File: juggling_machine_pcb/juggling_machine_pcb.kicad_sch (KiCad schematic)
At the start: 14 parts, among them J1 Conn_01x08, J2 Conn_01x08, J3 Conn_01x08, J4 Conn_01x08, J5 servo 1, J6 servo 2, J7 24v input, J8 5v input, J9 24v out for input to buck

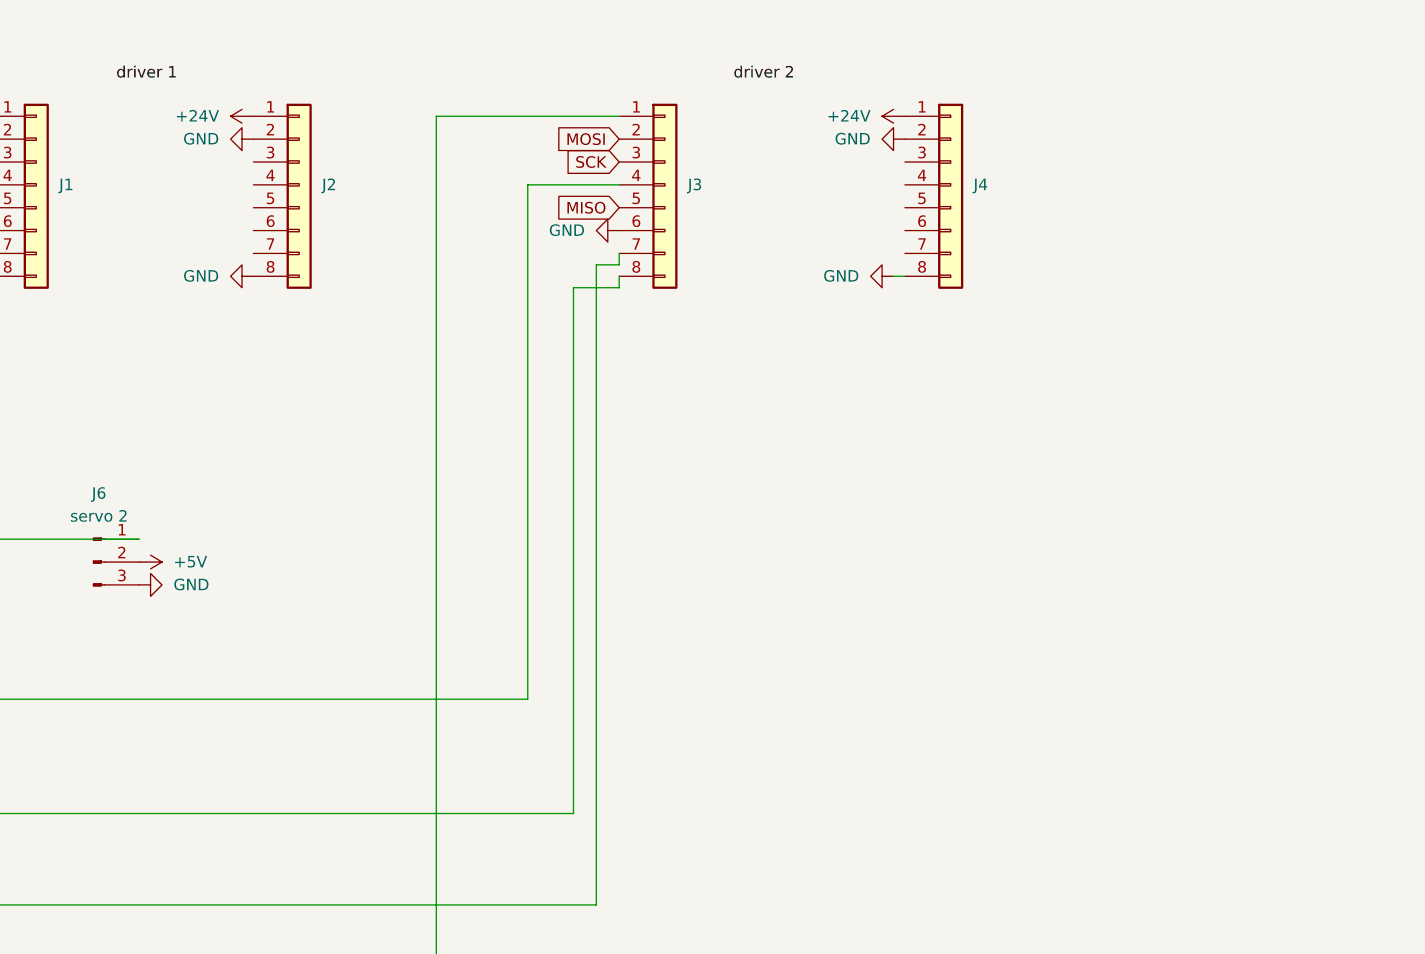
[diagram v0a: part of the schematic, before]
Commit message: added bom and updated pcb
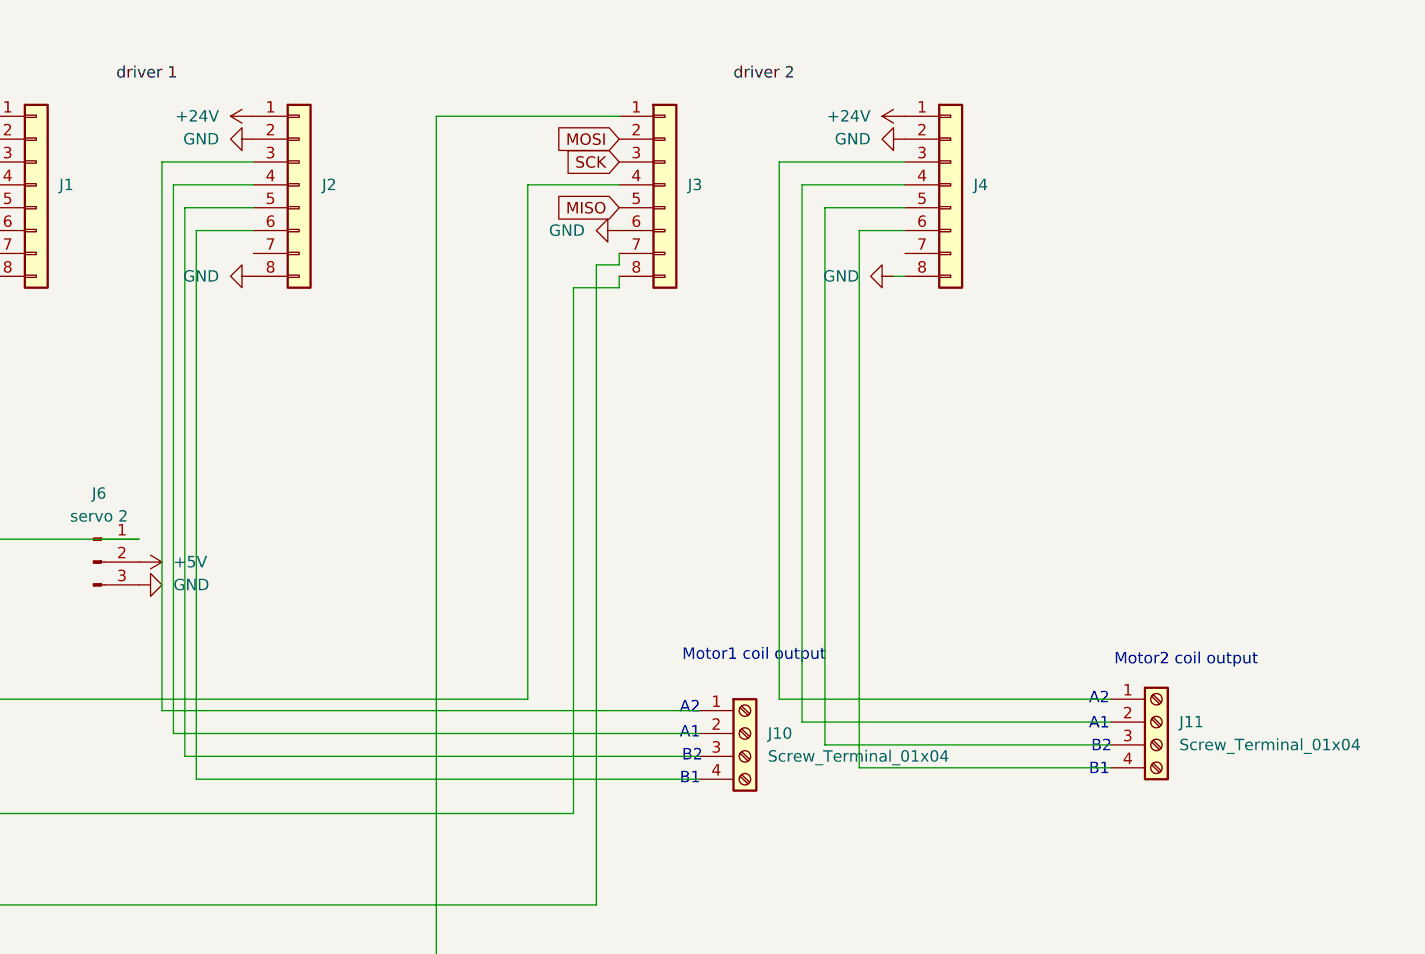
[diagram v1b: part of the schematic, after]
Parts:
- added J10, J11: Screw_Terminal_01x04, TerminalBlock_4Ucon:TerminalBlock_4Ucon_1x04_P3.50mm_Horizontal, symbol Connector:Screw_Terminal_01x04
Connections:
- net at J2.3 (Pin_3): now also J10.1 (Pin_1)
- net at J2.4 (Pin_4): now also J10.2 (Pin_2)
- net at J2.5 (Pin_5): now also J10.3 (Pin_3)
- net at J2.6 (Pin_6): now also J10.4 (Pin_4)
- net at J4.3 (Pin_3): now also J11.1 (Pin_1)
- net at J4.4 (Pin_4): now also J11.2 (Pin_2)
- net at J4.5 (Pin_5): now also J11.3 (Pin_3)
- net at J4.6 (Pin_6): now also J11.4 (Pin_4)
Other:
- note added: "A1"
- note added: "A2"
- note added: "B1"
- note added: "B2"
- note added: "Motor1 coil output"
- note added: "Motor2 coil output"

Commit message: added new BOM, plus updated pcb
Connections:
- net at A1.11 (GPIO8): no longer J3.1 (Pin_1)
- net CSN 2: now reaches A1.17 (GPIO13), J3.4 (Pin_4)
- net STEP 2: now reaches A1.20 (GPIO15), J3.7 (Pin_7)
- net DIR 2: now reaches A1.19 (GPIO14), J3.8 (Pin_8)
- net Servo 2: now reaches A1.27 (GPIO21), J6.1 (Pin_1)
- net STEP 1: now reaches A1.14 (GPIO10), J1.7 (Pin_7)
- net DIR 1: now reaches A1.15 (GPIO11), J1.8 (Pin_8)
- net CSN 1: now reaches A1.22 (GPIO17), J1.4 (Pin_4)
- net EN 1: now reaches A1.26 (GPIO20), J1.1 (Pin_1)
- net Servo 1: now reaches A1.29 (GPIO22), J5.1 (Pin_1)
- net A2.2: now reaches J11.1 (Pin_1), J4.3 (Pin_3)
- net A1.2: now reaches J11.2 (Pin_2), J4.4 (Pin_4)
- net B2.2: now reaches J11.3 (Pin_3), J4.5 (Pin_5)
- net B1.2: now reaches J11.4 (Pin_4), J4.6 (Pin_6)
- net A2.1: now reaches J10.1 (Pin_1), J2.3 (Pin_3)
- net A1.1: now reaches J10.2 (Pin_2), J2.4 (Pin_4)
- net B2.1: now reaches J10.3 (Pin_3), J2.5 (Pin_5)
- net B1.1: now reaches J10.4 (Pin_4), J2.6 (Pin_6)
- new net EN 2: J3.1 (Pin_1)
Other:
- note removed: "A1"
- note removed: "A2"
- note removed: "B1"
- note removed: "B2"
